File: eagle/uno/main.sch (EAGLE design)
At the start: 10 parts

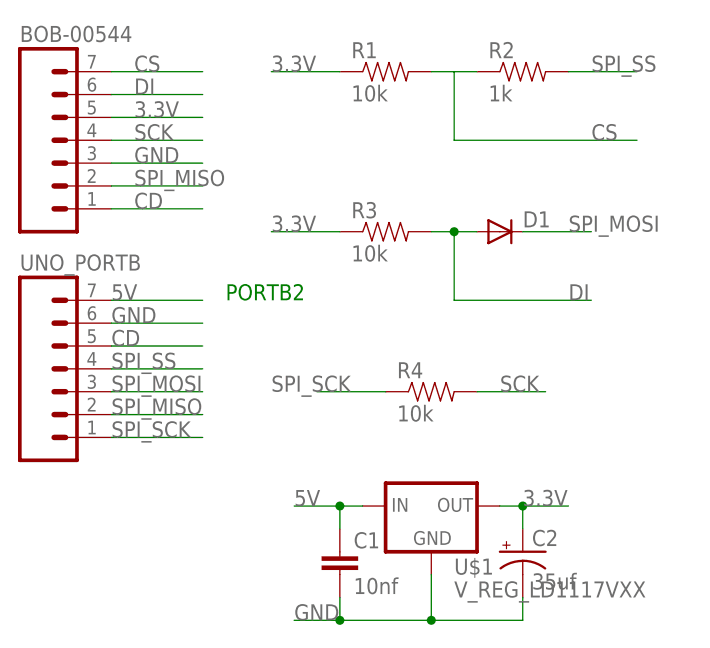
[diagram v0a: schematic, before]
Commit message: [ fix ] eagle/uno, voltage regulator footprint (TO220)
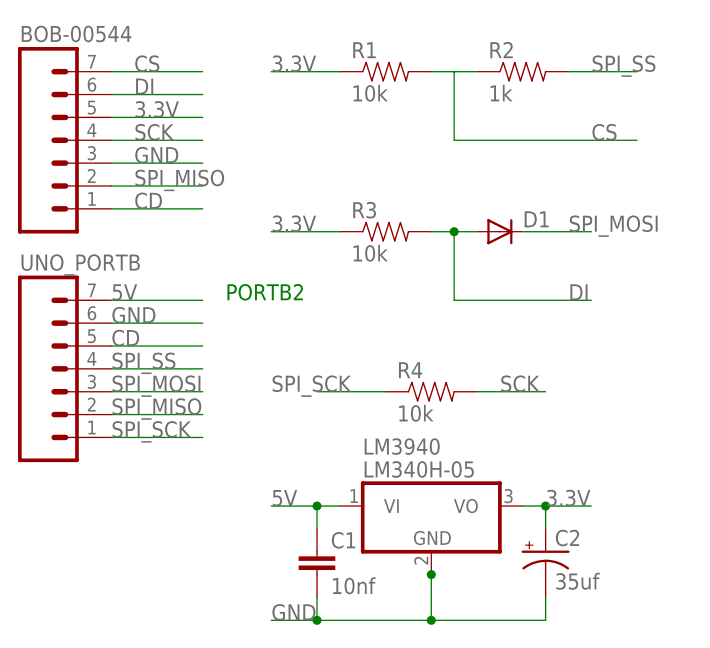
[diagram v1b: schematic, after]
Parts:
- removed U$1: V_REG_LD1117VXX, SparkFun:V_REG_LD1117VXX
- added LM3940: LM340H-05, linear:LM340H-05
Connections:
- net 3.3V: now also LM3940.VO; no longer U$1.OUT
- net 5V: now also LM3940.VI; no longer U$1.IN
- net GND: now also LM3940.GND; no longer U$1.GND
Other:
- moved on the sheet: C1, C2
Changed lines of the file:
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@@
 <setting verticaltext="up"/>
 </settings>
-<grid distance="2.54" unitdist="mm" unit="mm" style="lines" multiple="1" display="yes" altdistance="0.01" altunitdist="inch" altunit="inch"/>
+<grid distance="0.1" unitdist="inch" unit="inch" style="lines" multiple="1" display="no" altdistance="0.01" altunitdist="inch" altunit="inch"/>
 <layers>
 <layer number="1" name="Top" color="4" fill="1" visible="no" active="no"/>
@@
 <part name="C1" library="SparkFun" deviceset="CAP" device="PTH" value="10nf"/>
 <part name="C2" library="SparkFun" deviceset="CAP_POL" device="PTH1" value="35uf"/>
-<part name="U$1" library="SparkFun" deviceset="V_REG_LD1117VXX" device=""/>
+<part name="LM3940" library="linear" deviceset="LM340?-*" device="H" technology="05"/>
 </parts>
 <sheets>
@@
 <instance part="R4" gate="G$1" x="45.72" y="-2.54"/>
 <instance part="D1" gate="G$1" x="53.34" y="15.24"/>
-<instance part="C1" gate="G$1" x="35.56" y="-22.86"/>
-<instance part="C2" gate="G$1" x="55.88" y="-20.32"/>
-<instance part="U$1" gate="G$1" x="45.72" y="-15.24"/>
+<instance part="C1" gate="G$1" x="33.02" y="-22.86"/>
+<instance part="C2" gate="G$1" x="58.42" y="-20.32"/>
+<instance part="LM3940" gate="A" x="45.72" y="-15.24"/>
 </instances>
 <busses>
@@
 </segment>
 <segment>
-<pinref part="U$1" gate="G$1" pin="GND"/>
 <wire x1="45.72" y1="-22.86" x2="45.72" y2="-27.94" width="0.1524" layer="91"/>
-<wire x1="45.72" y1="-27.94" x2="35.56" y2="-27.94" width="0.1524" layer="91"/>
-<label x="30.48" y="-27.94" size="1.778" layer="95"/>
+<wire x1="45.72" y1="-27.94" x2="33.02" y2="-27.94" width="0.1524" layer="91"/>
+<label x="27.94" y="-27.94" size="1.778" layer="95"/>
 <pinref part="C2" gate="G$1" pin="-"/>
-<wire x1="35.56" y1="-27.94" x2="30.48" y2="-27.94" width="0.1524" layer="91"/>
-<wire x1="55.88" y1="-25.4" x2="55.88" y2="-27.94" width="0.1524" layer="91"/>
-<wire x1="45.72" y1="-27.94" x2="55.88" y2="-27.94" width="0.1524" layer="91"/>
+<wire x1="33.02" y1="-27.94" x2="27.94" y2="-27.94" width="0.1524" layer="91"/>
+<wire x1="58.42" y1="-25.4" x2="58.42" y2="-27.94" width="0.1524" layer="91"/>
+<wire x1="45.72" y1="-27.94" x2="58.42" y2="-27.94" width="0.1524" layer="91"/>
 <junction x="45.72" y="-27.94"/>
 <pinref part="C1" gate="G$1" pin="2"/>
-<wire x1="35.56" y1="-25.4" x2="35.56" y2="-27.94" width="0.1524" layer="91"/>
-<junction x="35.56" y="-27.94"/>
+<wire x1="33.02" y1="-25.4" x2="33.02" y2="-27.94" width="0.1524" layer="91"/>
+<junction x="33.02" y="-27.94"/>
+<pinref part="LM3940" gate="A" pin="GND"/>
+<junction x="45.72" y="-22.86"/>
 </segment>
 <segment>
@@
 <net name="5V" class="0">
 <segment>
-<pinref part="U$1" gate="G$1" pin="IN"/>
-<wire x1="38.1" y1="-15.24" x2="35.56" y2="-15.24" width="0.1524" layer="91"/>
-<label x="30.48" y="-15.24" size="1.778" layer="95"/>
+<wire x1="35.56" y1="-15.24" x2="33.02" y2="-15.24" width="0.1524" layer="91"/>
+<label x="27.94" y="-15.24" size="1.778" layer="95"/>
 <pinref part="C1" gate="G$1" pin="1"/>
-<wire x1="35.56" y1="-15.24" x2="30.48" y2="-15.24" width="0.1524" layer="91"/>
-<wire x1="35.56" y1="-17.78" x2="35.56" y2="-15.24" width="0.1524" layer="91"/>
-<junction x="35.56" y="-15.24"/>
+<wire x1="33.02" y1="-15.24" x2="27.94" y2="-15.24" width="0.1524" layer="91"/>
+<wire x1="33.02" y1="-17.78" x2="33.02" y2="-15.24" width="0.1524" layer="91"/>
+<junction x="33.02" y="-15.24"/>
+<pinref part="LM3940" gate="A" pin="VI"/>
 </segment>
 <segment>
@@
 <net name="3.3V" class="0">
 <segment>
-<pinref part="U$1" gate="G$1" pin="OUT"/>
-<wire x1="53.34" y1="-15.24" x2="55.88" y2="-15.24" width="0.1524" layer="91"/>
-<label x="55.88" y="-15.24" size="1.778" layer="95"/>
+<wire x1="55.88" y1="-15.24" x2="58.42" y2="-15.24" width="0.1524" layer="91"/>
+<label x="58.42" y="-15.24" size="1.778" layer="95"/>
 <pinref part="C2" gate="G$1" pin="+"/>
-<wire x1="55.88" y1="-15.24" x2="60.96" y2="-15.24" width="0.1524" layer="91"/>
-<wire x1="55.88" y1="-17.78" x2="55.88" y2="-15.24" width="0.1524" layer="91"/>
-<junction x="55.88" y="-15.24"/>
-</segment>
-<segment>
+<wire x1="58.42" y1="-15.24" x2="63.5" y2="-15.24" width="0.1524" layer="91"/>
+<wire x1="58.42" y1="-17.78" x2="58.42" y2="-15.24" width="0.1524" layer="91"/>
+<junction x="58.42" y="-15.24"/>
+<pinref part="LM3940" gate="A" pin="VO"/>
+</segment>
+<segment>
